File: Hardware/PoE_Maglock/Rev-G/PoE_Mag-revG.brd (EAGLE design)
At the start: 72.8 x 54.6 mm, 91 parts, among them IC2 ATMEGA32U4-MU, J11 1X2-3.5MM, J14 1X2-3.5MM, J15 1X2-3.5MM, J16 1X2-3.5MM, J17 1X2-3.5MM, J2 1X2-3.5MM, J3 1X2-3.5MM, J4 1X2-3.5MM, J5 1X2-3.5MM, J6 10103594-0001LF, Q1 35A/25V/8.5mΩ, Q3 35A/25V/8.5mΩ, Q5 35A/25V/8.5mΩ, Q6 35A/25V/8.5mΩ, SW1 SPST_TACT-KMR2, U4 W5500, X2 J1011FHY931147C, Y4 8MHz

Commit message: HEEP-1046 added terminal block silks and ground cheese vias for mag
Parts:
- moved J11 7.33 mm to (60.0, 50.8)
- moved D11 1.27 mm to (60.6, 38.8)
- moved J2 1.27 mm to (69.8, 41.9)
- moved J4 1.27 mm to (69.8, 25.4)
- moved Q1 1.27 mm to (61.6, 43.2)
- moved Q3 1.27 mm to (61.6, 34.3)
- moved D10 1.27 mm to (60.6, 11.0)
- moved D8 1.27 mm to (60.5, 29.7)
- moved D9 1.27 mm to (60.6, 20.5)
- moved J5 1.27 mm to (69.8, 17.1)
- moved Q5 1.27 mm to (61.6, 25.1)
- moved Q6 1.27 mm to (61.6, 15.9)
- moved J3 1.27 mm to (69.8, 33.7)
- moved X4 0.64 mm to (1.27, 22.9)
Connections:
- net GND: now also J11.1; no longer J11.2
- net VBAT: now also J11.2; no longer J11.1
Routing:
- net GND: vias 58 -> 94
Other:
- board text added: "3v3 A0 GND"
- board text added: "RX TX GND 3v3"
- board text added: "SCL SDA GND 3v3"
- board text added: "VCC"
- board text removed: "0"
- board text removed: "5"
- board text removed: "6"
- board text removed: "7"
- board text removed: "8"

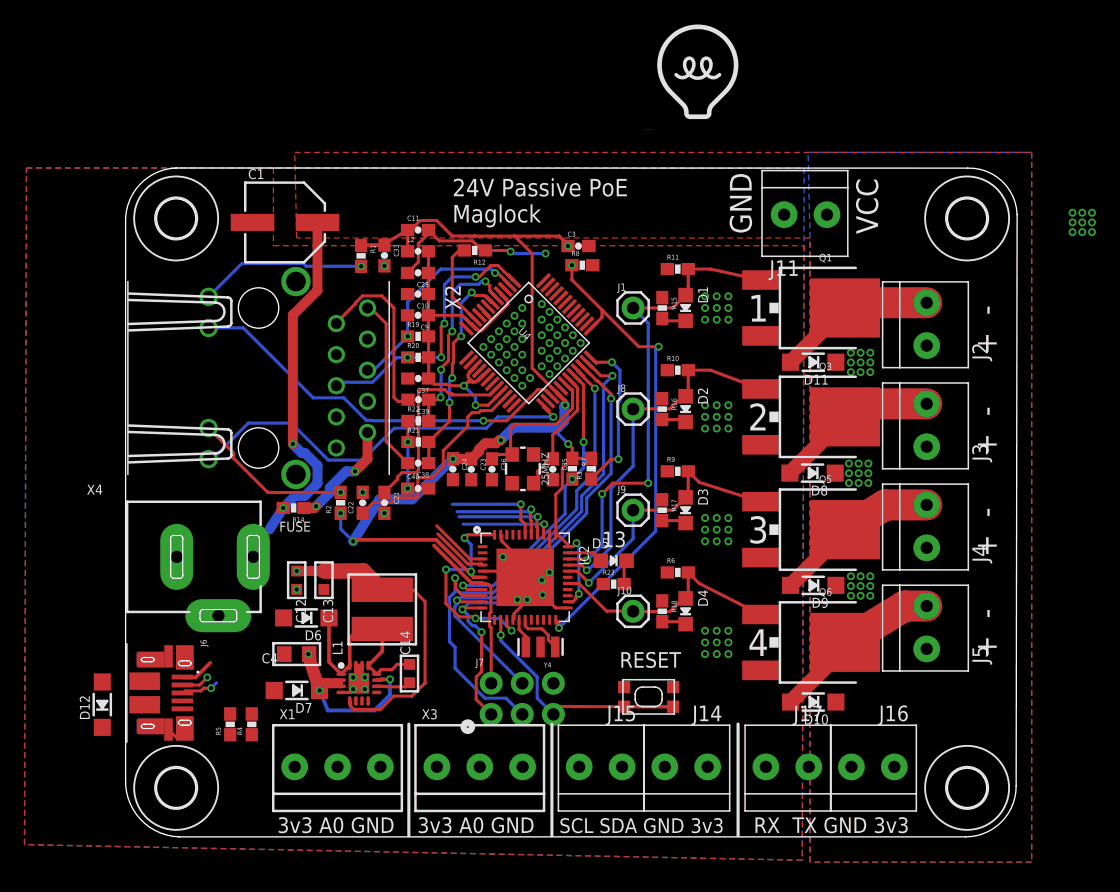
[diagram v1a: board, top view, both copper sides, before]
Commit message: HEEP-1046 allowed for more ground plane @ ethernet jack
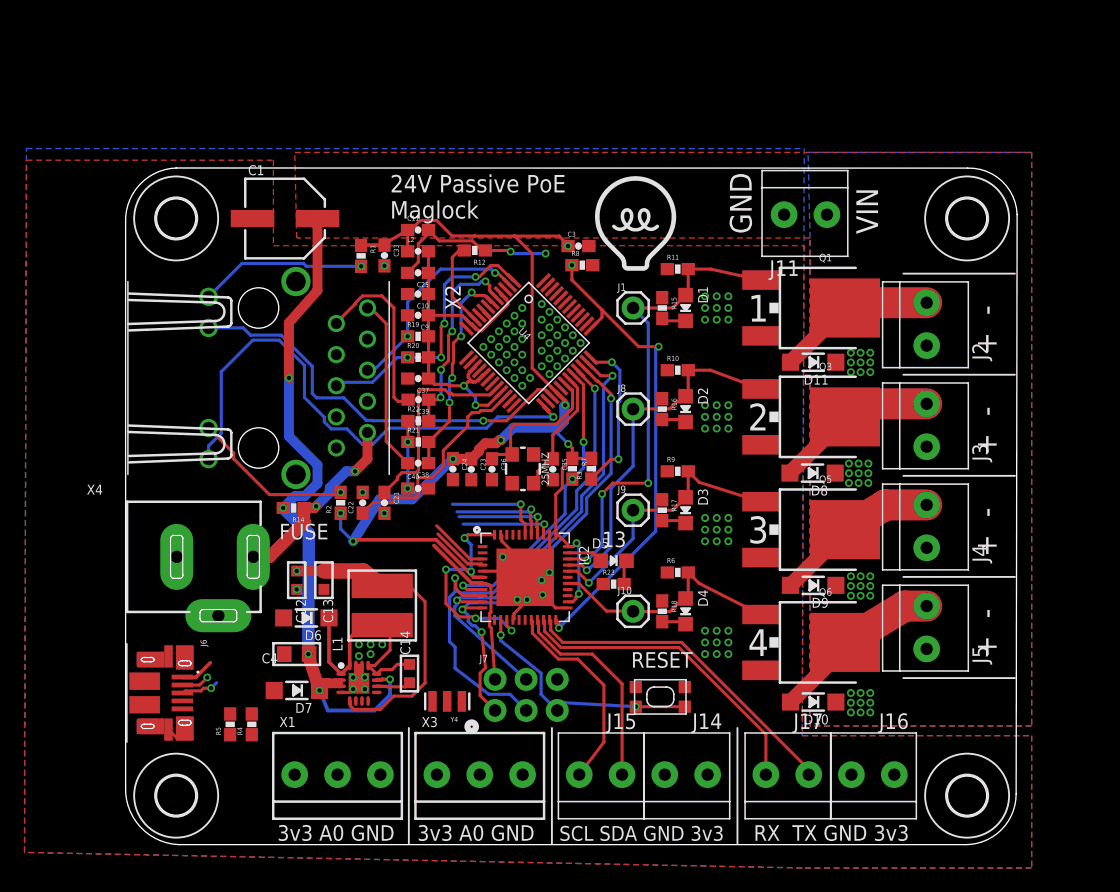
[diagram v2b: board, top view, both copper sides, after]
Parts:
- removed D12: PMEG4030ER, microbuilder:SOD-123
- moved U$15 13.4 mm to (41.6, 45.4)
- moved Y4 8.82 mm to (30.7, 11.1)
- moved SW1 0.95 mm to (48.1, 11.4)
- moved H2 0.64 mm to (8.57, 3.37)
- moved H4 0.64 mm to (73.1, 3.37)
- moved J14 0.63 mm to (50.2, 5.08)
- moved J15 0.63 mm to (43.2, 5.08)
- moved J16 0.63 mm to (65.4, 5.08)
- moved J17 0.63 mm to (58.4, 5.08)
- moved X1 0.63 mm to (21.7, 5.08)
- moved X3 0.63 mm to (33.4, 5.08)
- moved J7 0.45 mm to (37.1, 11.6)
- moved C1 0.32 mm to (17.5, 50.5)
- moved L1 0.32 mm to (25.4, 18.9)
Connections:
- removed net N$1: D12.A, X4.PWR
- net POE+: now also X4.PWR; no longer D12.C
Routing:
- net 1/TX: track 0.00 -> 27.3 mm
- net 0/RX: track 0.00 -> 25.8 mm
- net 2/SDA: track 0.00 -> 17.0 mm
- net 3/SCL: track 0.00 -> 16.7 mm
- net VBAT: track 52.0 -> 63.1 mm
- net LNKLED: track 33.7 -> 43.8 mm
- net POE+: track 9.23 -> 15.7 mm
- net N$12: track 3.89 -> 0.00 mm
- net RST: track 23.5 -> 20.2 mm, vias 1 -> 2
- net N$11: track 2.46 -> 0.00 mm
- net N$16: track 18.7 -> 20.7 mm
- net ACTLED: track 32.5 -> 33.8 mm
- net GND: vias 94 -> 99
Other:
- board size 72.8 x 54.6 mm -> 72.8 x 55.2 mm
- board text added: "VIN"
- board text removed: "VCC"

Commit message: HEEP-1046 done for now. dylan to review
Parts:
- moved Y4 11.3 mm to (42.0, 11.3), turned to 270 degrees
- moved J7 1.27 mm to (35.9, 11.6)
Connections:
- net A0: now also X3.2
- net A1: now also X1.2
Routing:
- net +3V3: track 136.5 -> 206.4 mm
- net D+: track 4.71 -> 41.2 mm, vias 0 -> 2
- net D-: track 4.87 -> 38.6 mm, vias 0 -> 2
- net A1: track 7.95 -> 38.0 mm
- net VBUS: track 16.5 -> 45.6 mm
- net A0: track 7.51 -> 30.4 mm
- net N$11: track 0.00 -> 10.7 mm
- net A2: track 8.29 -> 0.00 mm, vias 1 -> 0
- net A3: track 8.22 -> 0.00 mm, vias 1 -> 0
- net N$12: track 0.00 -> 7.83 mm
- net N$13: track 2.29 -> 6.65 mm, vias 1 -> 0
- net GND: track 50.3 -> 54.5 mm, vias 99 -> 103
- net N$6: track 3.12 -> 4.74 mm, vias 1 -> 0
- net MOSI: track 39.1 -> 38.2 mm
- net SCK: track 44.4 -> 43.6 mm
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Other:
- board text added: "3v3 A1 GND"
